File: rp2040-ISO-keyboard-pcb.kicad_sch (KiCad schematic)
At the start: 86 parts, among them J1 USB_C_Receptacle_USB2.0, U1 SRV05-4, U2 RP2040, U3 IS313741A, U4 XC6206, U5 W25Q128JVS, U6 SN74LV1T34DCKR, Y1 12MHz

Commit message: some layouts done
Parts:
- removed R41, R42, R44, R45, R48, R49: 20k, Resistor_SMD:R_0603_1608Metric, symbol Device:R_Small
- removed R43, R47, R50: 51k, Resistor_SMD:R_0603_1608Metric, symbol Device:R_Small
- removed R51: 100k, Capacitor_SMD:C_0402_1005Metric, symbol Device:R_Small
- removed U6: SN74LV1T34DCKR, Package_TO_SOT_SMD:SOT-353_SC-70-5, symbol Bonsai_C4:SN74LV1T34DCKR
- added J2: Conn_01x04, Connector_PinHeader_2.54mm:PinHeader_1x04_P2.54mm_Vertical, symbol Connector_Generic:Conn_01x04
- renumbered C21 to C20, C22 to C21, C23 to C22, C24 to C23, C20 to C24, R37 to R36, R38 to R37, R39 to R38, R40 to R39, R46 to R40, R36 to R41
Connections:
- net +3V3: now also J2.1 (Pin_1)
- net GND: now also J2.4 (Pin_4)
- net SWCLK: now reaches U2.24 (SWCLK)
- net SWCLK: now also J2.2 (Pin_2)
- net SWDIO: now reaches U2.25 (SWD)
- net SWDIO: now also J2.3 (Pin_3)
- net RGB: no longer names the net of U2.4 (GPIO2)
- no-connect marks 13 -> 21
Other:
- moved on the sheet: C22, C23, C24, R40, R41, U5, Y1, btn2

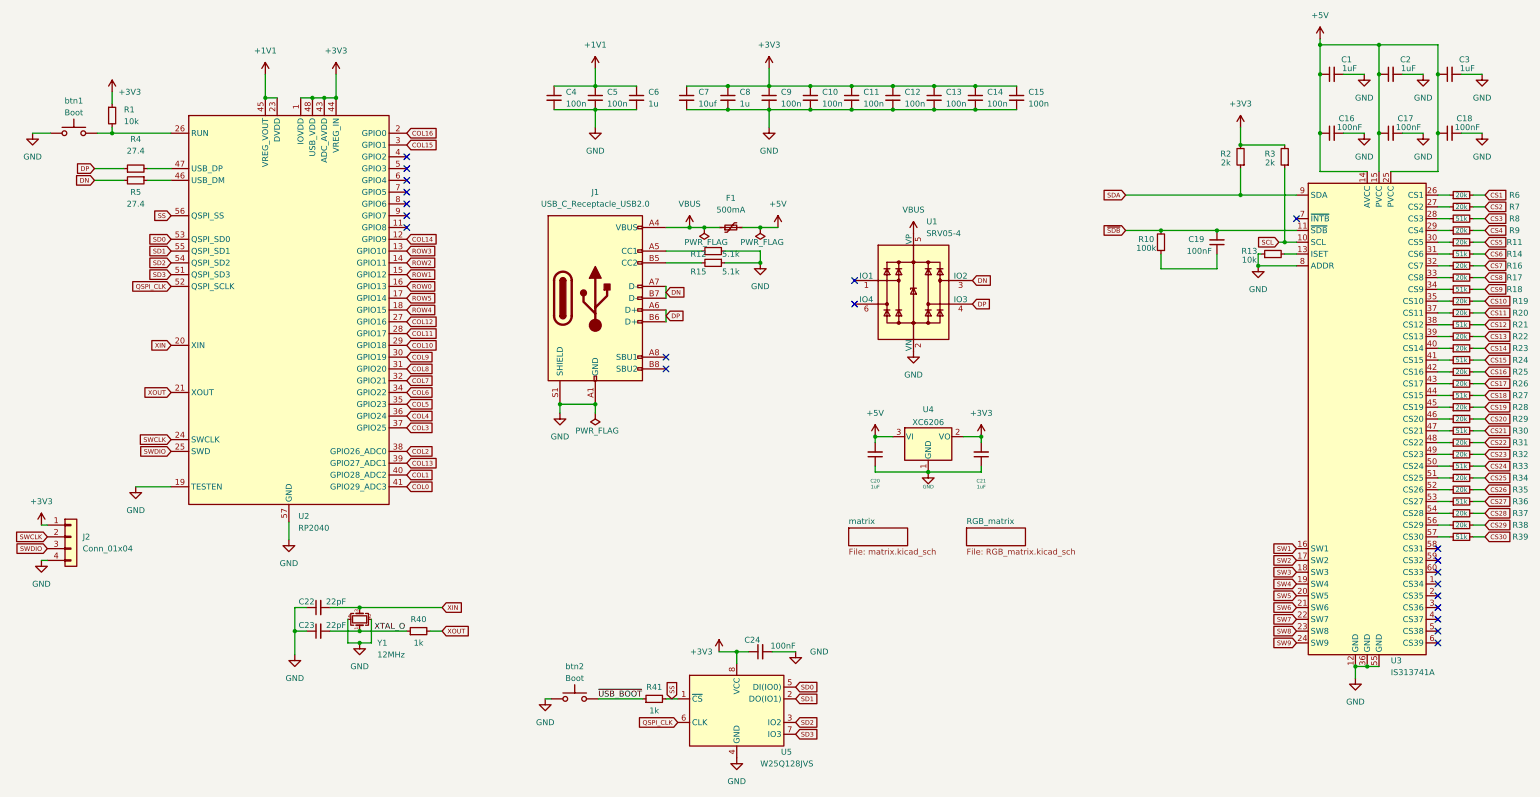
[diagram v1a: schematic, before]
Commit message: improved rgb schematic
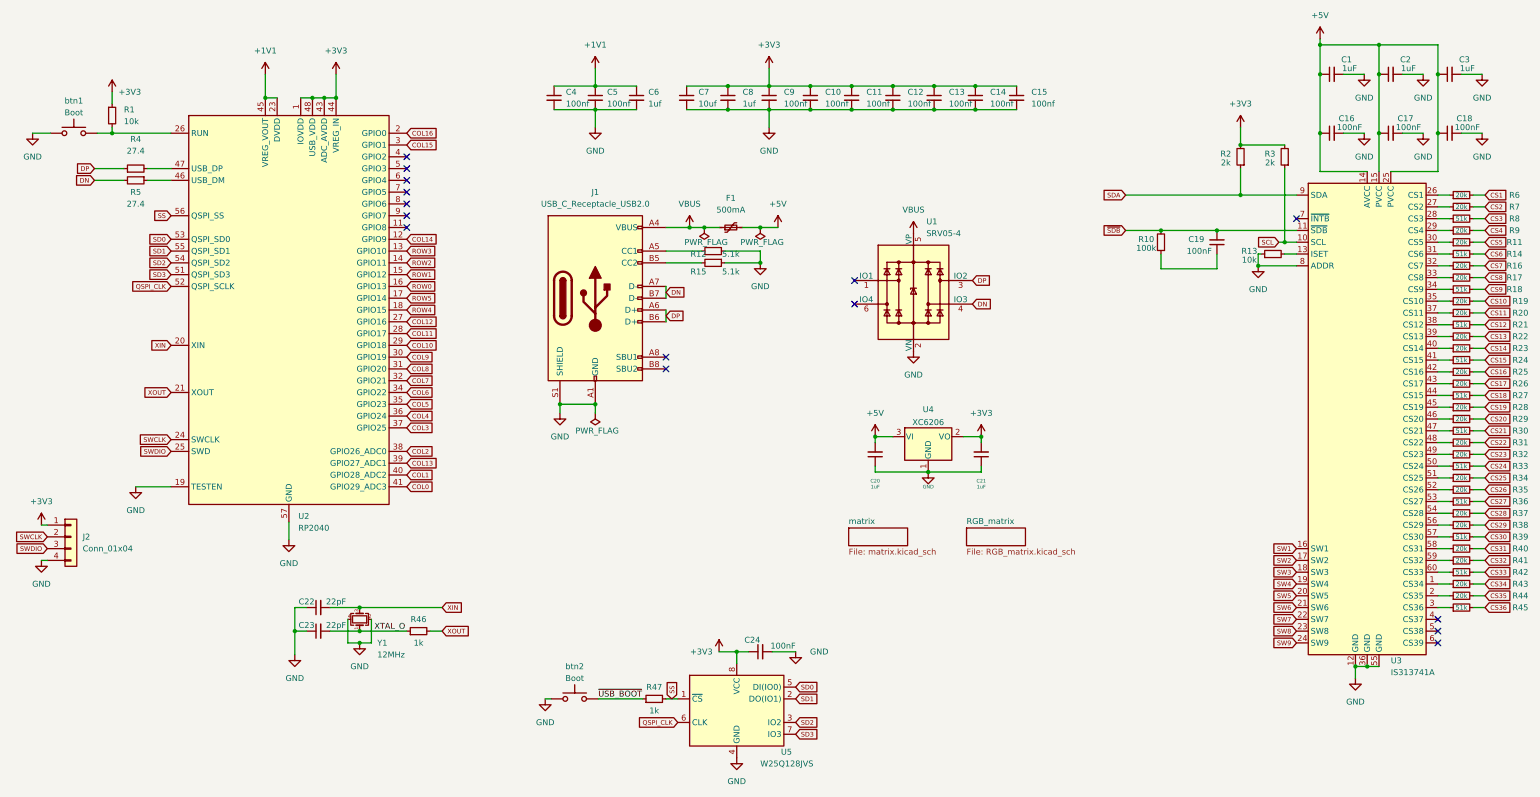
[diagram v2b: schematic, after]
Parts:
- added R40, R41, R43, R44: 20k, Resistor_SMD:R_0603_1608Metric, symbol Device:R_Small
- added R42, R45: 51k, Resistor_SMD:R_0603_1608Metric, symbol Device:R_Small
- C10, C11, C12, C13, C14, C15, C4, C5, C9: value 100n -> 100nf
- C6, C8: value 1u -> 1uf
- J1: footprint Connector_USB:USB_C_Receptacle_HRO_TYPE-C-31-M-12 -> marbastlib-various:USB_C_Receptacle_HRO_TYPE-C-31-M-14
- renumbered R40 to R46, R41 to R47
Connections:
- net DN: now also U1.4 (IO3); no longer U1.3 (IO2)
- net DP: now also U1.3 (IO2); no longer U1.4 (IO3)
- net at U3.1 (CS34): now also R43.1
- net at U3.2 (CS35): now also R44.1
- net at U3.3 (CS36): now also R45.1
- net at U3.58 (CS31): now also R40.1
- net at U3.59 (CS32): now also R41.1
- net at U3.60 (CS33): now also R42.1
- new net CS31: R40.2
- new net CS32: R41.2
- new net CS33: R42.2
- new net CS34: R43.2
- new net CS35: R44.2
- new net CS36: R45.2
- no-connect marks 21 -> 15

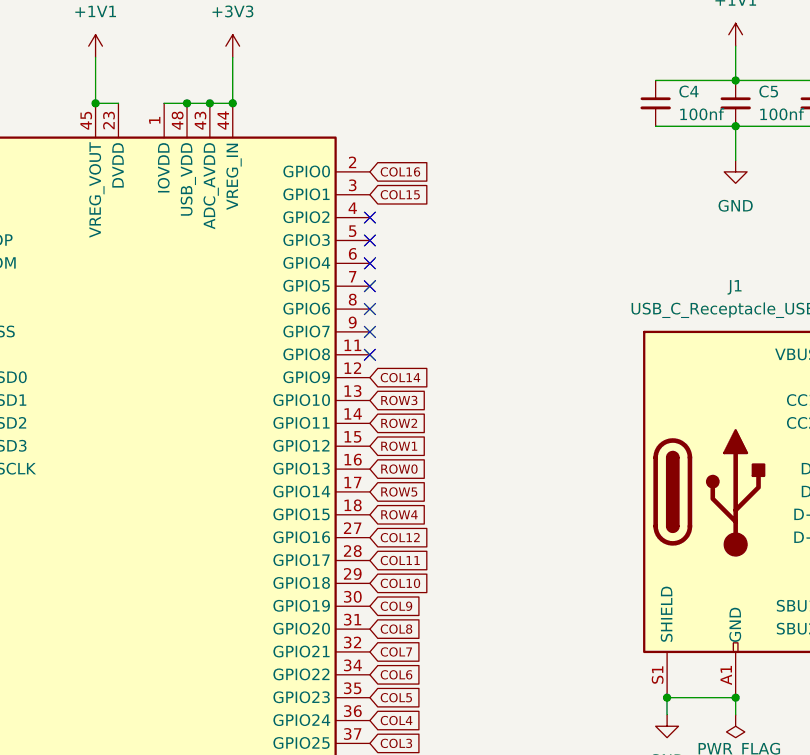
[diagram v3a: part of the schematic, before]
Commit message: wiring components
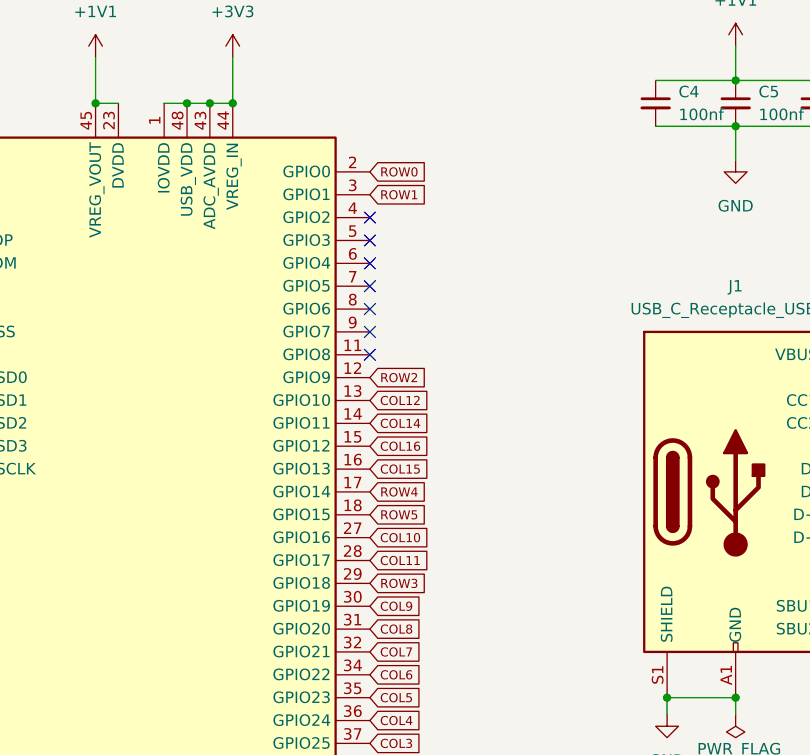
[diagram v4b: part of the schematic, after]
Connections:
- net COL10: now also U2.27 (GPIO16); no longer U2.29 (GPIO18)
- net COL12: now also U2.13 (GPIO10); no longer U2.27 (GPIO16)
- net COL14: now also U2.14 (GPIO11); no longer U2.12 (GPIO9)
- net COL15: now also U2.16 (GPIO13); no longer U2.3 (GPIO1)
- net COL16: now also U2.15 (GPIO12); no longer U2.2 (GPIO0)
- net ROW0: now also U2.2 (GPIO0); no longer U2.16 (GPIO13)
- net ROW1: now also U2.3 (GPIO1); no longer U2.15 (GPIO12)
- net ROW2: now also U2.12 (GPIO9); no longer U2.14 (GPIO11)
- net ROW3: now also U2.29 (GPIO18); no longer U2.13 (GPIO10)
- net ROW4: now also U2.17 (GPIO14); no longer U2.18 (GPIO15)
- net ROW5: now also U2.18 (GPIO15); no longer U2.17 (GPIO14)
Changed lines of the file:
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@@
     )
   )
-  (global_label "COL14" (shape input) (at 107.95 67.31 0) (fields_autoplaced)
-    (effects (font (size 1 1)) (justify left))
-    (property "Intersheet References" "${INTERSHEET_REFS}" (id 0) (at 114.6119 67.2475 0)
+  (global_label "COL14" (shape input) (at 107.95 72.39 0) (fields_autoplaced)
+    (effects (font (size 1 1)) (justify left))
+    (property "Intersheet References" "${INTERSHEET_REFS}" (id 0) (at 114.6119 72.3275 0)
       (effects (font (size 1 1)) (justify left) hide)
     )
@@
     )
   )
-  (global_label "COL10" (shape input) (at 107.95 90.17 0) (fields_autoplaced)
-    (effects (font (size 1 1)) (justify left))
-    (property "Intersheet References" "${INTERSHEET_REFS}" (id 0) (at 114.6119 90.1075 0)
+  (global_label "COL10" (shape input) (at 107.95 85.09 0) (fields_autoplaced)
+    (effects (font (size 1 1)) (justify left))
+    (property "Intersheet References" "${INTERSHEET_REFS}" (id 0) (at 114.6119 85.0275 0)
       (effects (font (size 1 1)) (justify left) hide)
     )
@@
     )
   )
-  (global_label "ROW3" (shape input) (at 107.95 69.85 0) (fields_autoplaced)
-    (effects (font (size 1 1)) (justify left))
-    (property "Intersheet References" "${INTERSHEET_REFS}" (id 0) (at 113.9929 69.7875 0)
+  (global_label "ROW3" (shape input) (at 107.95 90.17 0) (fields_autoplaced)
+    (effects (font (size 1 1)) (justify left))
+    (property "Intersheet References" "${INTERSHEET_REFS}" (id 0) (at 113.9929 90.1075 0)
       (effects (font (size 1 1)) (justify left) hide)
     )
@@
     )
   )
-  (global_label "COL16" (shape input) (at 107.95 44.45 0) (fields_autoplaced)
-    (effects (font (size 1 1)) (justify left))
-    (property "Intersheet References" "${INTERSHEET_REFS}" (id 0) (at 114.6119 44.3875 0)
+  (global_label "COL16" (shape input) (at 107.95 74.93 0) (fields_autoplaced)
+    (effects (font (size 1 1)) (justify left))
+    (property "Intersheet References" "${INTERSHEET_REFS}" (id 0) (at 114.6119 74.8675 0)
       (effects (font (size 1 1)) (justify left) hide)
     )
@@
     )
   )
-  (global_label "ROW1" (shape input) (at 107.95 74.93 0) (fields_autoplaced)
-    (effects (font (size 1 1)) (justify left))
-    (property "Intersheet References" "${INTERSHEET_REFS}" (id 0) (at 113.9929 74.8675 0)
+  (global_label "ROW1" (shape input) (at 107.95 46.99 0) (fields_autoplaced)
+    (effects (font (size 1 1)) (justify left))
+    (property "Intersheet References" "${INTERSHEET_REFS}" (id 0) (at 113.9929 46.9275 0)
       (effects (font (size 1 1)) (justify left) hide)
     )
@@
     )
   )
-  (global_label "ROW2" (shape input) (at 107.95 72.39 0) (fields_autoplaced)
-    (effects (font (size 1 1)) (justify left))
-    (property "Intersheet References" "${INTERSHEET_REFS}" (id 0) (at 113.9929 72.3275 0)
+  (global_label "ROW2" (shape input) (at 107.95 67.31 0) (fields_autoplaced)
+    (effects (font (size 1 1)) (justify left))
+    (property "Intersheet References" "${INTERSHEET_REFS}" (id 0) (at 113.9929 67.2475 0)
       (effects (font (size 1 1)) (justify left) hide)
     )
@@
     )
   )
-  (global_label "COL15" (shape input) (at 107.95 46.99 0) (fields_autoplaced)
-    (effects (font (size 1 1)) (justify left))
-    (property "Intersheet References" "${INTERSHEET_REFS}" (id 0) (at 114.6119 46.9275 0)
+  (global_label "COL15" (shape input) (at 107.95 77.47 0) (fields_autoplaced)
+    (effects (font (size 1 1)) (justify left))
+    (property "Intersheet References" "${INTERSHEET_REFS}" (id 0) (at 114.6119 77.4075 0)
       (effects (font (size 1 1)) (justify left) hide)
     )
@@
     )
   )
-  (global_label "COL12" (shape input) (at 107.95 85.09 0) (fields_autoplaced)
-    (effects (font (size 1 1)) (justify left))
-    (property "Intersheet References" "${INTERSHEET_REFS}" (id 0) (at 114.6119 85.0275 0)
+  (global_label "COL12" (shape input) (at 107.95 69.85 0) (fields_autoplaced)
+    (effects (font (size 1 1)) (justify left))
+    (property "Intersheet References" "${INTERSHEET_REFS}" (id 0) (at 114.6119 69.7875 0)
       (effects (font (size 1 1)) (justify left) hide)
     )
@@
     )
   )
-  (global_label "ROW5" (shape input) (at 107.95 80.01 0) (fields_autoplaced)
+  (global_label "ROW5" (shape input) (at 107.95 82.55 0) (fields_autoplaced)
+    (effects (font (size 1 1)) (justify left))
+    (property "Intersheet References" "${INTERSHEET_REFS}" (id 0) (at 113.9929 82.4875 0)
+      (effects (font (size 1 1)) (justify left) hide)
+    )
+  )
+  (global_label "SD1" (shape input) (at 191.77 166.37 0) (fields_autoplaced)
+    (effects (font (size 1 1)) (justify left))
+    (property "Intersheet References" "${INTERSHEET_REFS}" (id 0) (at 196.5748 166.3075 0)
+      (effects (font (size 1 1)) (justify left) hide)
+    )
+  )
+  (global_label "ROW4" (shape input) (at 107.95 80.01 0) (fields_autoplaced)
     (effects (font (size 1 1)) (justify left))
     (property "Intersheet References" "${INTERSHEET_REFS}" (id 0) (at 113.9929 79.9475 0)
@@
     )
   )
-  (global_label "SD1" (shape input) (at 191.77 166.37 0) (fields_autoplaced)
-    (effects (font (size 1 1)) (justify left))
-    (property "Intersheet References" "${INTERSHEET_REFS}" (id 0) (at 196.5748 166.3075 0)
-      (effects (font (size 1 1)) (justify left) hide)
-    )
-  )
-  (global_label "ROW4" (shape input) (at 107.95 82.55 0) (fields_autoplaced)
-    (effects (font (size 1 1)) (justify left))
-    (property "Intersheet References" "${INTERSHEET_REFS}" (id 0) (at 113.9929 82.4875 0)
-      (effects (font (size 1 1)) (justify left) hide)
-    )
-  )
   (global_label "CS24" (shape input) (at 340.36 116.205 0) (fields_autoplaced)
     (effects (font (size 1 1)) (justify left))
@@
     )
   )
-  (global_label "ROW0" (shape input) (at 107.95 77.47 0) (fields_autoplaced)
-    (effects (font (size 1 1)) (justify left))
-    (property "Intersheet References" "${INTERSHEET_REFS}" (id 0) (at 113.9929 77.4075 0)
-      (effects (font (size 1 1)) (justify left) hide)
-    )
+  (global_label "ROW0" (shape input) (at 107.95 44.45 0) (fields_autoplaced)
+    (effects (font (size 1 1)) (justify left))
+    (property "Intersheet References" "${INTERSHEET_REFS}" (id 0) (at 113.9929 44.3875 0)
+      (effects (font (size 1 1)) (justify left) hide)
+    )

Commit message: more routing done
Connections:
- net COL13: now also U2.34 (GPIO22); no longer U2.39 (GPIO27_ADC1)
- net COL2: now also U2.39 (GPIO27_ADC1); no longer U2.38 (GPIO26_ADC0)
- net COL3: now also U2.38 (GPIO26_ADC0); no longer U2.37 (GPIO25)
- net COL4: now also U2.37 (GPIO25); no longer U2.36 (GPIO24)
- net COL5: now also U2.36 (GPIO24); no longer U2.35 (GPIO23)
- net COL6: now also U2.35 (GPIO23); no longer U2.34 (GPIO22)
- net COL7: now also U2.31 (GPIO20); no longer U2.32 (GPIO21)
- net COL8: now also U2.32 (GPIO21); no longer U2.31 (GPIO20)
- net ROW2: now also U2.5 (GPIO3); no longer U2.12 (GPIO9)
